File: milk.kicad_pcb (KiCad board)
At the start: 2 copper layers, 19.2 x 39.4 mm, 21 parts, among them J1 USB_C_Receptacle_USB2.0, J3 RGB, J4 PB3|PB4, SW1 SW_Push, SW2 SW_Push, SW3 SW_Push_Reset, U1 ATtiny85-20SU

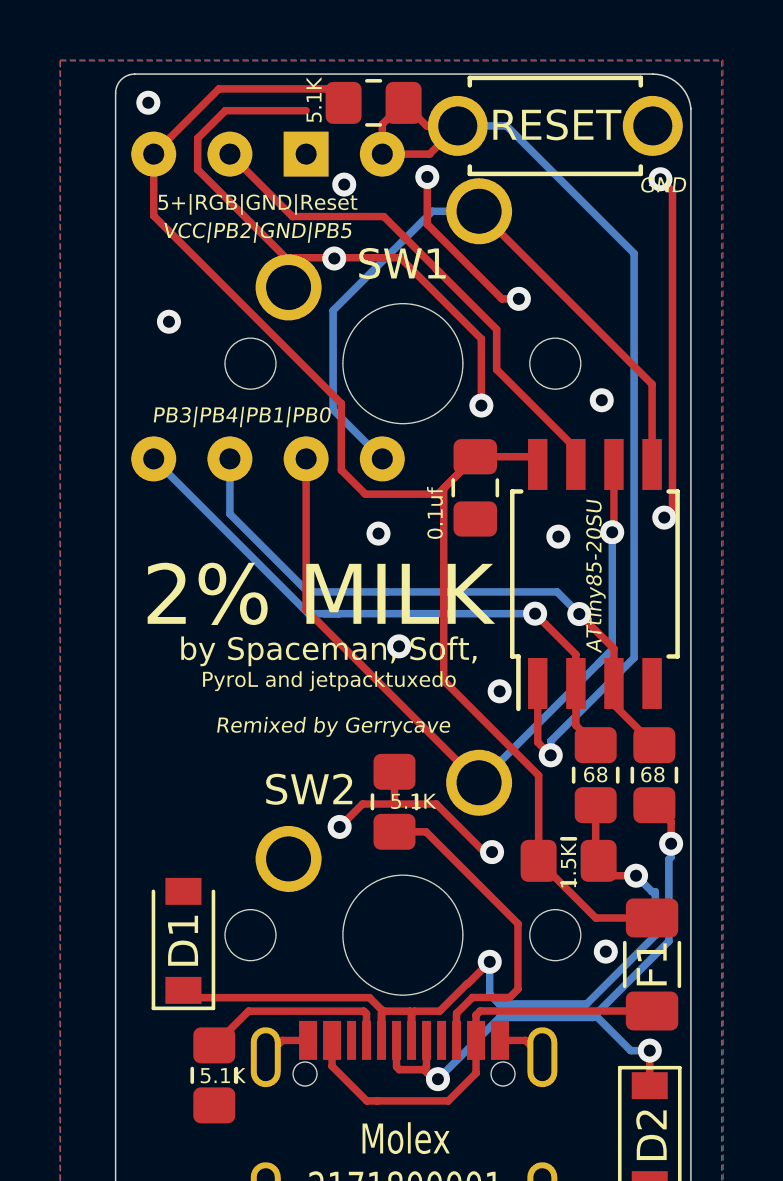
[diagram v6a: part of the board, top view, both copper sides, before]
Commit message: Change programming header for a DIP-8 package, compatible with ATtiny85-20PU
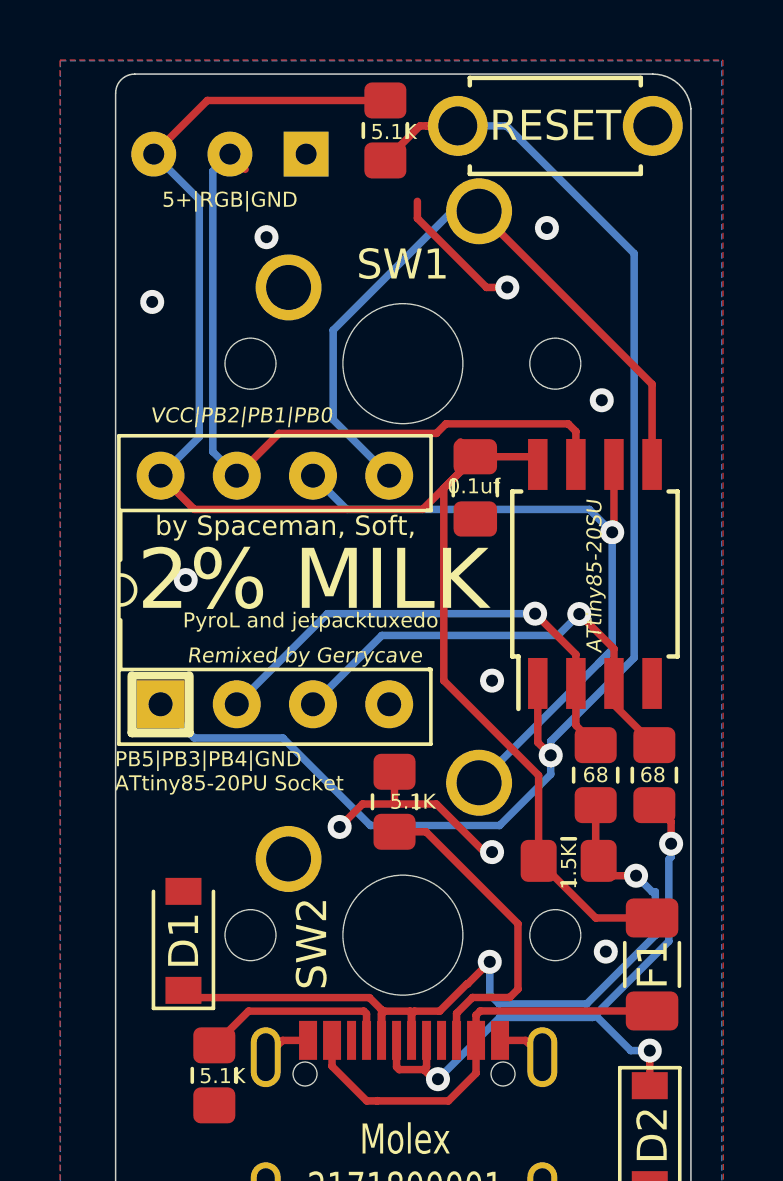
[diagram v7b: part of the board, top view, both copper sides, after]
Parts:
- removed H1, H2: Switch Pin 1, TestPoint:TestPoint_THTPad_D1.5mm_Drill0.7mm
- removed H3: Reset, TestPoint:TestPoint_THTPad_D1.5mm_Drill0.7mm
- removed J4: PB3|PB4, Connector_PinHeader_2.54mm:PinHeader_1x02_P2.54mm_Vertical
- added J3: DIP-8_W7.62mm_Socket, Package_DIP:DIP-8_W7.62mm_Socket, F.Cu at (172.9, 81.8)
- moved R6 1.00 mm to (180.4, 62.7), turned to 90 degrees
- renumbered J3 to J2
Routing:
- net GND: track 46.9 -> 15.2 mm, vias 17 -> 10
- net RST: track 35.1 -> 48.0 mm
- net RGB: track 18.3 -> 26.3 mm
- net +5V: track 48.0 -> 54.9 mm
- net PB4: track 20.5 -> 15.5 mm
- net PB3: track 20.6 -> 16.4 mm
- net PB1: track 26.4 -> 23.9 mm
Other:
- board text added: "5+|RGB|GND"
- board text added: "PB5|PB3|PB4|GND ATtiny85-20PU Socket"
- board text added: "VCC|PB2|PB1|PB0"
- board text removed: "5+|RGB|GND|Reset"
- board text removed: "GND"
- board text removed: "PB3|PB4|PB1|PB0"
- board text removed: "VCC|PB2|GND|PB5"

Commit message: wip
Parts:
- added REF**: LED_SK6812MINI_PLCC4_3.5x3.5mm_P1.75mm, LED_SMD:LED_SK6812MINI_PLCC4_3.5x3.5mm_P1.75mm, F.Cu at (206.0, 73.0)
- moved J3 8.12 mm to (180.7, 84.2), turned to 180 degrees
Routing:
- net GND: vias 10 -> 8
- net (no net): vias 0 -> 2
